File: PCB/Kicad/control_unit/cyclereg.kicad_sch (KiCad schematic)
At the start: 7 parts

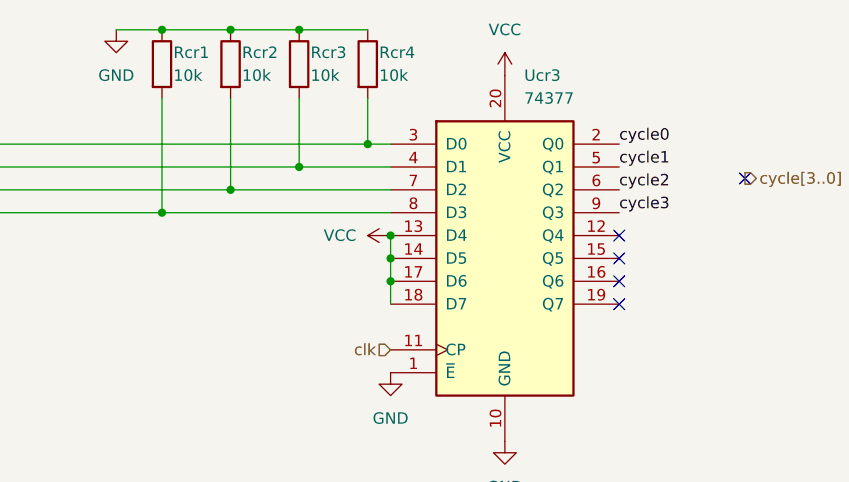
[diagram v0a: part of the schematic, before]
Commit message: control unit logic routing done
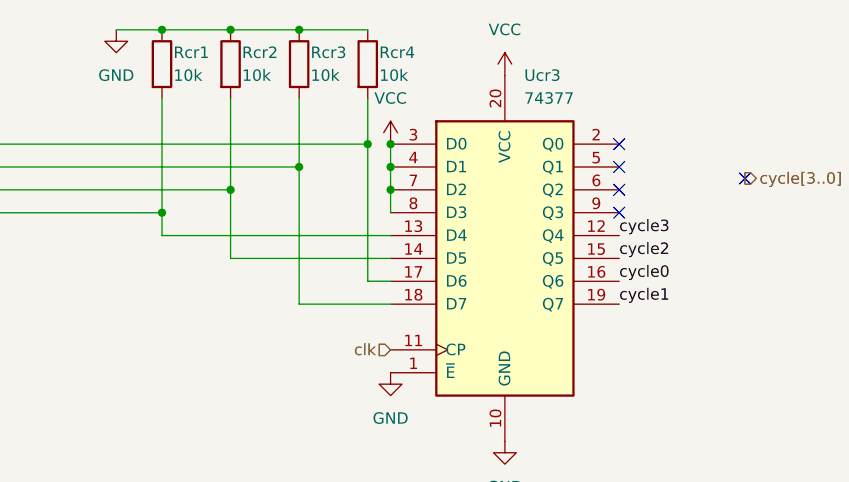
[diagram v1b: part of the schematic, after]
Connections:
- net VCC: now also Ucr3.3 (D0), Ucr3.4 (D1), Ucr3.7 (D2), Ucr3.8 (D3); no longer Ucr3.13 (D4), Ucr3.14 (D5), Ucr3.17 (D6), Ucr3.18 (D7)
- net cycle0: now also Ucr3.16 (Q6); no longer Ucr3.2 (Q0)
- net cycle1: now also Ucr3.19 (Q7); no longer Ucr3.5 (Q1)
- net cycle2: now also Ucr3.15 (Q5); no longer Ucr3.6 (Q2)
- net cycle3: now also Ucr3.12 (Q4); no longer Ucr3.9 (Q3)
- net at Rcr4.2, Ucr2.4 (Za): now also Ucr3.17 (D6); no longer Ucr3.3 (D0)
- net at Rcr3.2, Ucr2.7 (Zb): now also Ucr3.18 (D7); no longer Ucr3.4 (D1)
- net at Rcr2.2, Ucr2.12 (Zc): now also Ucr3.14 (D5); no longer Ucr3.7 (D2)
- net at Rcr1.2, Ucr2.9 (Zd): now also Ucr3.13 (D4); no longer Ucr3.8 (D3)
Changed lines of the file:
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@@
-	)
-	(junction
-		(at 203.2 88.9)
-		(diameter 0)
-		(color 0 0 0 0)
 	)
 	(junction
@@
 	)
 	(junction
-		(at 203.2 93.98)
+		(at 203.2 83.82)
 		(diameter 0)
 		(color 0 0 0 0)
@@
 	)
 	(junction
+		(at 203.2 78.74)
+		(diameter 0)
+		(color 0 0 0 0)
+	)
+	(junction
 		(at 82.55 101.6)
 		(diameter 0)
@@
 	)
 	(junction
+		(at 185.42 83.82)
+		(diameter 0)
+		(color 0 0 0 0)
+	)
+	(junction
 		(at 177.8 66.04)
 		(diameter 0)
@@
 	)
 	(junction
-		(at 203.2 91.44)
-		(diameter 0)
-		(color 0 0 0 0)
-	)
-	(junction
 		(at 193.04 81.28)
 		(diameter 0)
@@
 	)
 	(junction
-		(at 185.42 83.82)
+		(at 203.2 81.28)
 		(diameter 0)
 		(color 0 0 0 0)
 	)
 	(no_connect
-		(at 228.6 93.98)
-	)
-	(no_connect
-		(at 228.6 91.44)
+		(at 228.6 81.28)
 	)
 	(no_connect
@@
 	)
 	(no_connect
-		(at 228.6 96.52)
+		(at 228.6 78.74)
 	)
 	(no_connect
-		(at 228.6 88.9)
+		(at 228.6 83.82)
+	)
+	(no_connect
+		(at 228.6 86.36)
 	)
 	(wire
@@
 	(wire
 		(pts
-			(xy 200.66 78.74) (xy 203.2 78.74)
-		)
-		(stroke
-			(width 0)
-			(type default)
-		)
-	)
-	(wire
-		(pts
 			(xy 151.13 81.28) (xy 151.13 86.36)
 		)
@@
 	(wire
 		(pts
+			(xy 193.04 81.28) (xy 193.04 96.52)
+		)
+		(stroke
+			(width 0)
+			(type default)
+		)
+	)
+	(wire
+		(pts
 			(xy 107.95 78.74) (xy 116.84 78.74)
 		)
@@
 	(wire
 		(pts
-			(xy 203.2 88.9) (xy 203.2 91.44)
-		)
-		(stroke
-			(width 0)
-			(type default)
-		)
-	)
-	(wire
-		(pts
 			(xy 114.3 83.82) (xy 114.3 96.52)
 		)
@@
 	(wire
 		(pts
-			(xy 193.04 81.28) (xy 203.2 81.28)
+			(xy 185.42 83.82) (xy 185.42 91.44)
+		)
+		(stroke
+			(width 0)
+			(type default)
+		)
+	)
+	(wire
+		(pts
+			(xy 203.2 83.82) (xy 203.2 86.36)
+		)
+		(stroke
+			(width 0)
+			(type default)
+		)
+	)
+	(wire
+		(pts
+			(xy 203.2 81.28) (xy 203.2 83.82)
 		)
 		(stroke
@@
 	(wire
 		(pts
+			(xy 177.8 88.9) (xy 203.2 88.9)
+		)
+		(stroke
+			(width 0)
+			(type default)
+		)
+	)
+	(wire
+		(pts
 			(xy 113.03 104.14) (xy 124.46 104.14)
 		)
@@
 	(wire
 		(pts
-			(xy 203.2 86.36) (xy 177.8 86.36)
-		)
-		(stroke
-			(width 0)
-			(type default)
-		)
-	)
-	(wire
-		(pts
 			(xy 107.95 83.82) (xy 114.3 83.82)
 		)
@@
 	(wire
 		(pts
+			(xy 185.42 91.44) (xy 203.2 91.44)
+		)
+		(stroke
+			(width 0)
+			(type default)
+		)
+	)
+	(wire
+		(pts
 			(xy 200.66 73.66) (xy 200.66 78.74)
 		)
@@
 	(wire
 		(pts
+			(xy 177.8 86.36) (xy 177.8 88.9)
+		)
+		(stroke
+			(width 0)
+			(type default)
+		)
+	)
+	(wire
+		(pts
 			(xy 123.19 74.295) (xy 123.19 78.74)
 		)
@@
 	(wire
 		(pts
+			(xy 200.66 93.98) (xy 203.2 93.98)
+		)
+		(stroke
+			(width 0)
+			(type default)
+		)
+	)
+	(wire
+		(pts
 			(xy 123.19 101.6) (xy 124.46 101.6)
 		)
@@
 	(wire
 		(pts
-			(xy 185.42 83.82) (xy 203.2 83.82)
-		)
-		(stroke
-			(width 0)
-			(type default)
-		)
-	)
-	(wire
-		(pts
 			(xy 82.55 99.06) (xy 82.55 101.6)
 		)
@@
 	(wire
 		(pts
-			(xy 203.2 91.44) (xy 203.2 93.98)
-		)
-		(stroke
-			(width 0)
-			(type default)
-		)
-	)
-	(wire
-		(pts
 			(xy 113.03 86.36) (xy 113.03 104.14)
 		)
@@
 	(wire
 		(pts
-			(xy 203.2 93.98) (xy 203.2 96.52)
+			(xy 200.66 78.74) (xy 200.66 93.98)
+		)
+		(stroke
+			(width 0)
+			(type default)
+		)
+	)
+	(wire
+		(pts
+			(xy 203.2 78.74) (xy 203.2 81.28)
 		)
 		(stroke
@@
 		)
 	)
+	(wire
+		(pts
+			(xy 193.04 96.52) (xy 203.2 96.52)
+		)
+		(stroke
+			(width 0)
+			(type default)
+		)
+	)
 	(label "cycle2"
-		(at 228.6 83.82 0)
+		(at 228.6 91.44 0)
 		(effects
 			(font
@@
 	)
 	(label "cycle0"
-		(at 228.6 78.74 0)
+		(at 228.6 93.98 0)
 		(effects
 			(font
@@
 	)
 	(label "cycle3"
-		(at 228.6 86.36 0)
+		(at 228.6 88.9 0)
 		(effects
 			(font
@@
 	)
 	(label "cycle1"
-		(at 228.6 81.28 0)
+		(at 228.6 96.52 0)
 		(effects
 			(font
@@
 	)
 	(symbol
-		(lib_id "power:VCC")
-		(at 203.2 88.9 90)
-		(unit 1)
-		(body_style 1)
-		(exclude_from_sim no)
-		(in_bom yes)
-		(on_board yes)
-		(in_pos_files yes)
-		(dnp no)
-		(fields_autoplaced yes)
-		(property "Reference" "#PWR0207"
-			(at 207.01 88.9 0)
-			(hide yes)
-			(show_name no)
-			(do_not_autoplace no)
-			(effects
-				(font
-					(size 1.27 1.27)
-				)
-			)
-		)
-		(property "Value" "VCC"
-			(at 199.39 88.8999 90)
-			(show_name no)
-			(do_not_autoplace no)
-			(effects
-				(font
-					(size 1.27 1.27)
-				)
-				(justify left)
-			)
-		)
-		(property "Footprint" ""
-			(at 203.2 88.9 0)
-			(hide yes)
-			(show_name no)
-			(do_not_autoplace no)
-			(effects
-				(font
-					(size 1.27 1.27)
-				)
-			)
-		)
-		(property "Datasheet" ""
-			(at 203.2 88.9 0)
-			(hide yes)
-			(show_name no)
-			(do_not_autoplace no)
-			(effects
-				(font
-					(size 1.27 1.27)
-				)
-			)
-		)
-		(property "Description" "Power symbol creates a global label with name \"VCC\""
-			(at 203.2 88.9 0)
-			(hide yes)
-			(show_name no)
-			(do_not_autoplace no)
-			(effects
-				(font
-					(size 1.27 1.27)
-				)
-			)
-		)
-		(pin "1"
-		)
-		(instances
-			(project "control_unit"
-				(path "/dccec861-b967-466c-843e-d6d1ad6064ce/a601307c-be83-4128-aa2e-f19df4dff19c/9a79b597-abb2-44e5-893d-3b1e1cb1e119"
-					(reference "#PWR0207")
-					(unit 1)
-				)
-			)
-		)
-	)
-	(symbol
 		(lib_id "Device:R")
 		(at 200.66 69.85 0)
@@
 					(unit 1)
 				)
+			)
+		)
+	)
+	(symbol
+		(lib_id "power:VCC")
+		(at 203.2 78.74 0)
+		(unit 1)
+		(body_style 1)
+		(exclude_from_sim no)
+		(in_bom yes)
+		(on_board yes)
+		(in_pos_files yes)
+		(dnp no)
+		(fields_autoplaced yes)
+		(property "Reference" "#PWR0207"
+			(at 203.2 82.55 0)
+			(hide yes)
+			(show_name no)
+			(do_not_autoplace no)
+			(effects
+				(font
+					(size 1.27 1.27)
+				)
+			)
+		)
+		(property "Value" "VCC"
+			(at 203.2 73.66 0)
+			(show_name no)
+			(do_not_autoplace no)
+			(effects
+				(font
+					(size 1.27 1.27)
+				)
+			)
+		)
+		(property "Footprint" ""
+			(at 203.2 78.74 0)
+			(hide yes)
+			(show_name no)
+			(do_not_autoplace no)
+			(effects
+				(font
+					(size 1.27 1.27)
+				)
+			)
+		)
+		(property "Datasheet" ""
+			(at 203.2 78.74 0)
+			(hide yes)
+			(show_name no)
+			(do_not_autoplace no)
+			(effects
+				(font
+					(size 1.27 1.27)
+				)
+			)
+		)
+		(property "Description" "Power symbol creates a global label with name \"VCC\""
+			(at 203.2 78.74 0)
+			(hide yes)
+			(show_name no)
+			(do_not_autoplace no)
+			(effects
+				(font
+					(size 1.27 1.27)
+				)
+			)
+		)
+		(pin "1"
+		)
+		(instances
+			(project "control_unit"
+				(path "/dccec861-b967-466c-843e-d6d1ad6064ce/a601307c-be83-4128-aa2e-f19df4dff19c/9a79b597-abb2-44e5-893d-3b1e1cb1e119"
+					(reference "#PWR0207")
+					(unit 1)
+				)
